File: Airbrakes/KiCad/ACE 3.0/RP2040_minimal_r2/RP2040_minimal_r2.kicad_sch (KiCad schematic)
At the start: 45 parts, among them J1 USB_B_Micro, J2 Conn_01x02, J3 104031-0811, J4 Conn_02x18_Odd_Even, U1 NCP1117-3.3_SOT223, U2 W25Q128JVS, U3 RP2040, U4 BMI088, U5 BMP581, U6 BMM350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

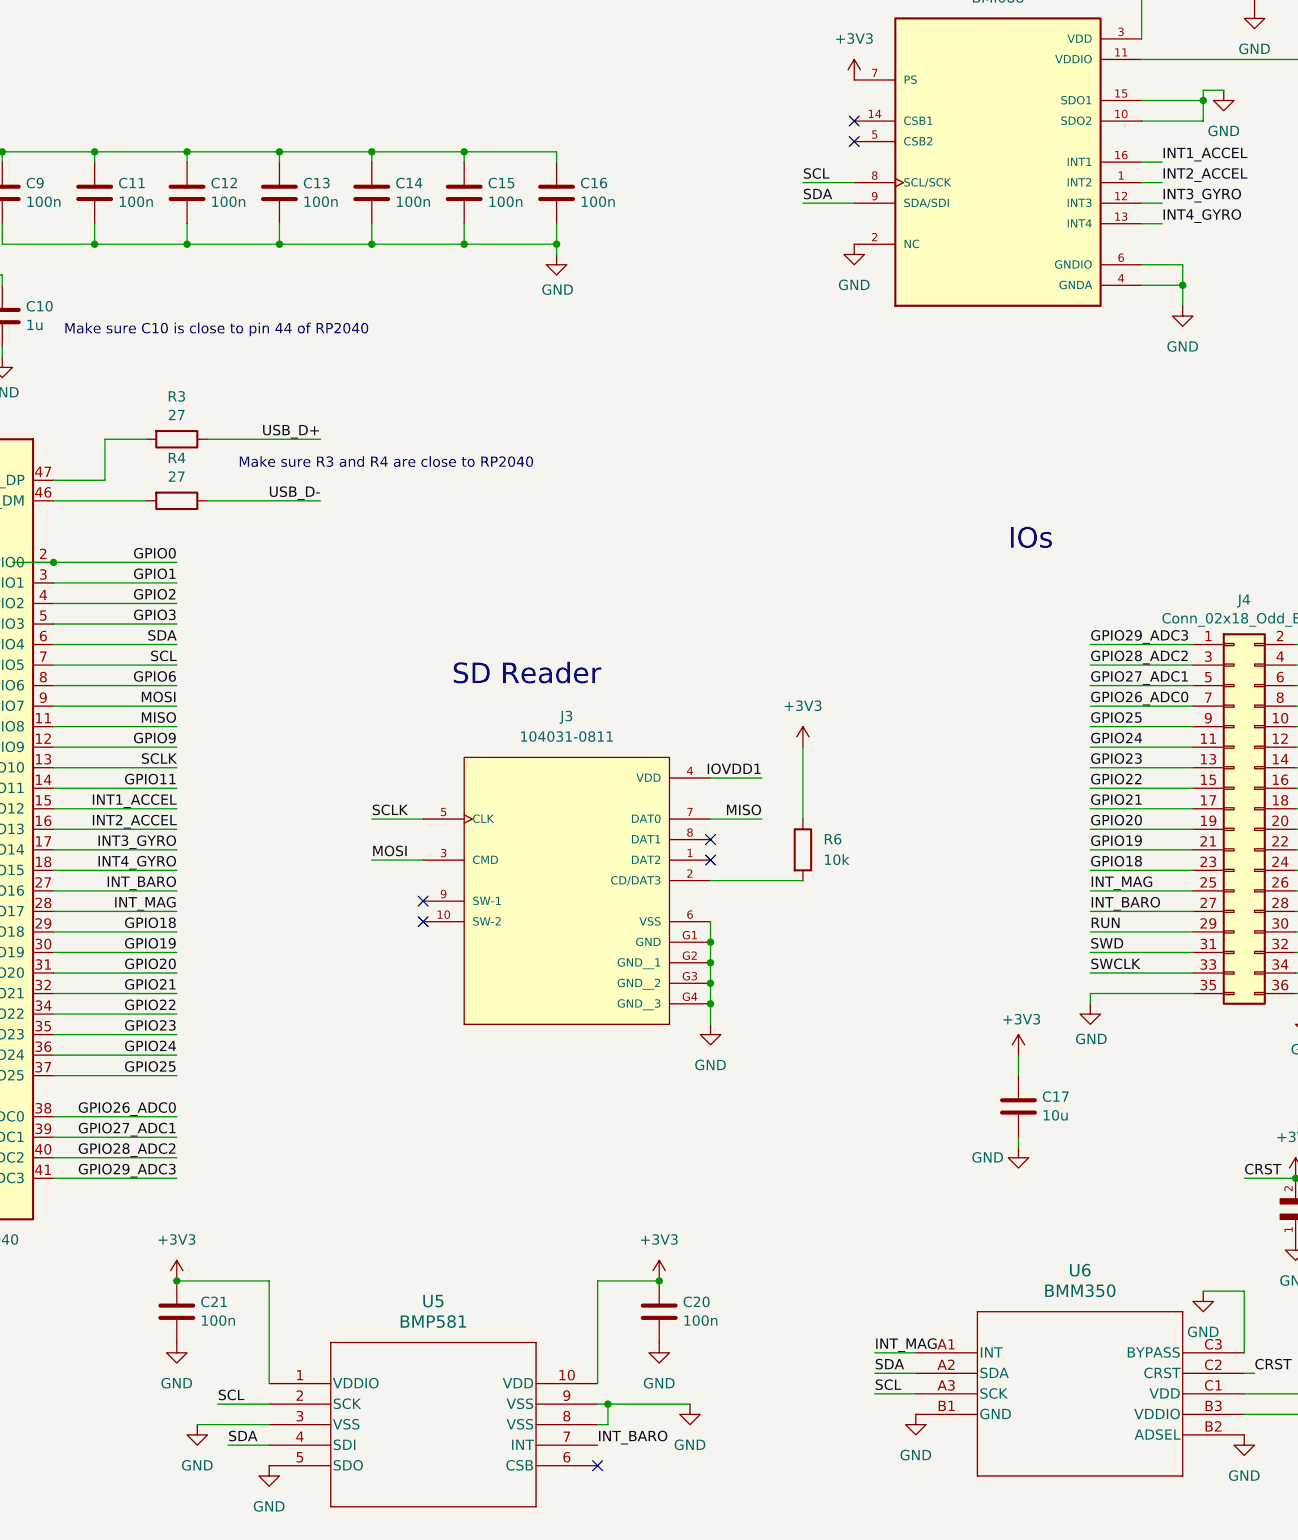
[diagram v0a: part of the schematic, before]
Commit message: Update footprint refs
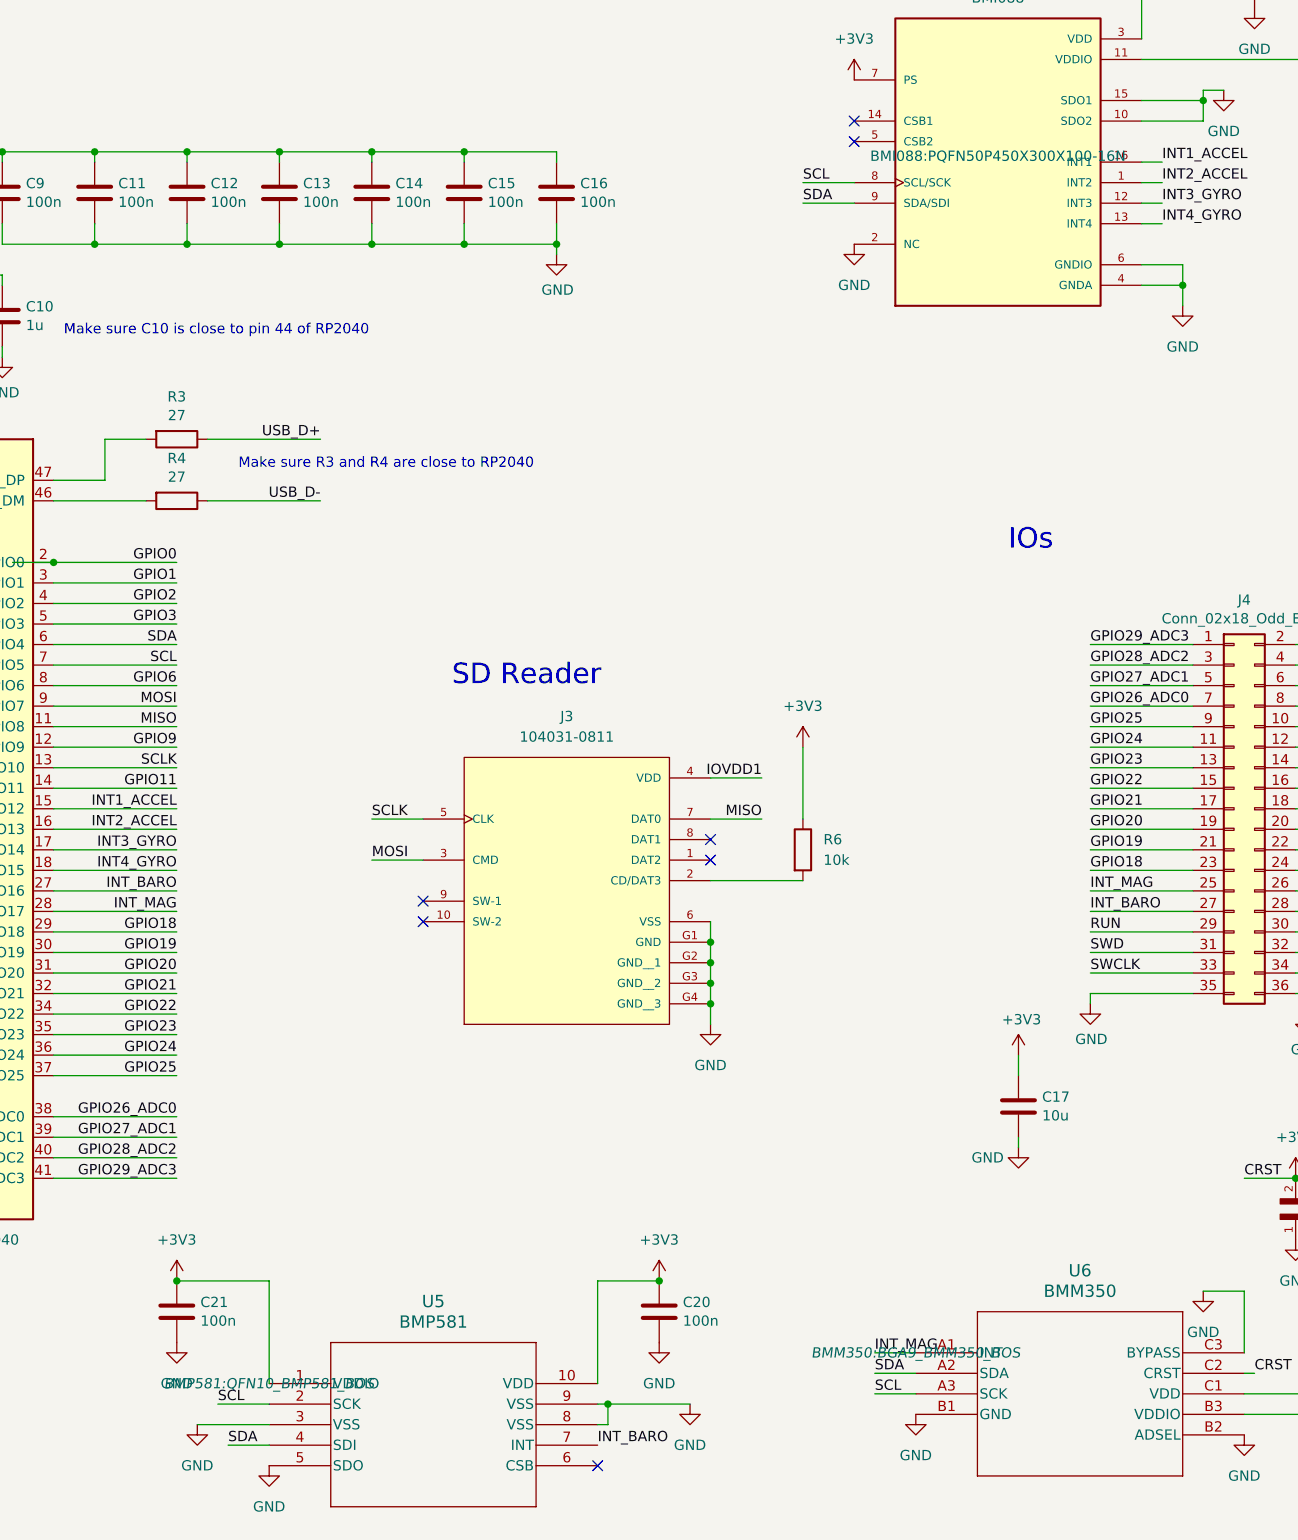
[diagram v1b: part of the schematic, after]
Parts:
- U5: footprint QFN10_BMP581_BOS -> BMP581:QFN10_BMP581_BOS
- U6: footprint BGA9_BMM350_BOS -> BMM350:BGA9_BMM350_BOS
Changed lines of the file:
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@@
 			)
 		)
-		(property "Footprint" "BGA9_BMM350_BOS"
+		(property "Footprint" "BMM350:BGA9_BMM350_BOS"
 			(at 336.55 209.55 0)
 			(effects
@@
 					(italic yes)
 				)
-				(hide yes)
 			)
 		)
@@
 				)
 				(justify bottom)
-				(hide yes)
 			)
 		)
@@
 			)
 		)
-		(property "Footprint" "QFN10_BMP581_BOS"
+		(property "Footprint" "BMP581:QFN10_BMP581_BOS"
 			(at 256.54 213.36 0)
 			(effects
@@
 					(italic yes)
 				)
-				(hide yes)
-			)
-		)
+			)
+		)

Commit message: buttons
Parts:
- removed J2: Conn_01x02, Connector_PinHeader_2.54mm:PinHeader_1x02_P2.54mm_Vertical, symbol Connector_Generic:Conn_01x02
- added U7, U8: B3U-1000P, Button_Switch_SMD:SW_SPST_B3U-1000P, symbol BOOT_Button:B3U-1000P
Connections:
- net GND: now also U7.1, U8.1
- net RUN: now also U8.2
- net ~{USB_BOOT}: now also U7.2
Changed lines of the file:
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@@
 	)
 	(junction
+		(at 142.24 165.1)
+		(diameter 0)
+		(color 0 0 0 0)
+	)
+	(junction
 		(at 384.81 144.78)
 		(diameter 0)
@@
 	(wire
 		(pts
-			(xy 166.37 165.1) (xy 152.4 165.1)
+			(xy 166.37 165.1) (xy 142.24 165.1)
 		)
 		(stroke
@@
 	(wire
 		(pts
-			(xy 31.75 128.27) (xy 33.02 128.27)
-		)
-		(stroke
-			(width 0)
-			(type default)
-		)
-	)
-	(wire
-		(pts
 			(xy 234.95 60.96) (xy 246.38 60.96)
 		)
@@
 	(wire
 		(pts
+			(xy 142.24 165.1) (xy 134.62 165.1)
+		)
+		(stroke
+			(width 0)
+			(type default)
+		)
+	)
+	(wire
+		(pts
 			(xy 104.14 102.87) (xy 104.14 101.6)
 		)
@@
 	(wire
 		(pts
-			(xy 33.02 128.27) (xy 33.02 129.54)
-		)
-		(stroke
-			(width 0)
-			(type default)
-		)
-	)
-	(wire
-		(pts
 			(xy 383.54 149.86) (xy 384.81 149.86)
 		)
@@
 	)
 	(label "RUN"
-		(at 152.4 165.1 0)
+		(at 134.62 165.1 0)
 		(fields_autoplaced yes)
 		(effects
@@
 	)
 	(symbol
-		(lib_id "Connector_Generic:Conn_01x02")
-		(at 26.67 125.73 0)
-		(mirror y)
-		(unit 1)
-		(exclude_from_sim no)
-		(in_bom yes)
-		(on_board yes)
-		(dnp no)
-		(property "Reference" "J2"
-			(at 25.4 121.92 0)
-			(effects
-				(font
-					(size 1.27 1.27)
-				)
-			)
-		)
-		(property "Value" "Conn_01x02"
-			(at 25.4 132.08 0)
-			(effects
-				(font
-					(size 1.27 1.27)
-				)
-			)
-		)
-		(property "Footprint" "Connector_PinHeader_2.54mm:PinHeader_1x02_P2.54mm_Vertical"
-			(at 26.67 125.73 0)
-			(effects
-				(font
-					(size 1.27 1.27)
-				)
-				(hide yes)
-			)
-		)
-		(property "Datasheet" "~"
-			(at 26.67 125.73 0)
-			(effects
-				(font
-					(size 1.27 1.27)
-				)
-				(hide yes)
-			)
-		)
-		(property "Description" ""
-			(at 26.67 125.73 0)
-			(effects
-				(font
-					(size 1.27 1.27)
-				)
-				(hide yes)
-			)
-		)
-		(pin "1"
-		)
-		(pin "2"
-		)
-		(instances
-			(project "RP2040_minimal_r2"
-				(path "/8c0b3d8b-46d3-4173-ab1e-a61765f77d61"
-					(reference "J2")
-					(unit 1)
-				)
-			)
-		)
-	)
-	(symbol
 		(lib_id "power:GND")
-		(at 33.02 129.54 0)
+		(at 31.75 166.37 0)
 		(unit 1)
 		(exclude_from_sim no)
@@
 		(dnp no)
 		(property "Reference" "#PWR02"
-			(at 33.02 135.89 0)
+			(at 31.75 172.72 0)
 			(effects
 				(font
@@
 		)
 		(property "Value" "GND"
-			(at 33.147 133.9342 0)
+			(at 31.877 170.7642 0)
 			(effects
 				(font
@@
 		)
 		(property "Footprint" ""
-			(at 33.02 129.54 0)
+			(at 31.75 166.37 0)
 			(effects
 				(font
@@
 		)
 		(property "Datasheet" ""
-			(at 33.02 129.54 0)
+			(at 31.75 166.37 0)
 			(effects
 				(font
@@
 		)
 		(property "Description" ""
-			(at 33.02 129.54 0)
+			(at 31.75 166.37 0)
 			(effects
 				(font
@@
 	)
 	(symbol
+		(lib_id "power:GND")
+		(at 142.24 205.74 0)
+		(unit 1)
+		(exclude_from_sim no)
+		(in_bom yes)
+		(on_board yes)
+		(dnp no)
+		(property "Reference" "#PWR021"
+			(at 142.24 212.09 0)
+			(effects
+				(font
+					(size 1.27 1.27)
+				)
+				(hide yes)
+			)
+		)
+		(property "Value" "GND"
+			(at 142.367 210.1342 0)
+			(effects
+				(font
+					(size 1.27 1.27)
+				)
+			)
+		)
+		(property "Footprint" ""
+			(at 142.24 205.74 0)
+			(effects
+				(font
+					(size 1.27 1.27)
+				)
+				(hide yes)
+			)
+		)
+		(property "Datasheet" ""
+			(at 142.24 205.74 0)
+			(effects
+				(font
+					(size 1.27 1.27)
+				)
+				(hide yes)
+			)
+		)
+		(property "Description" ""
+			(at 142.24 205.74 0)
+			(effects
+				(font
+					(size 1.27 1.27)
+				)
+				(hide yes)
+			)
+		)
+		(pin "1"
+		)
+		(instances
+			(project "RP2040_minimal_r2"
+				(path "/8c0b3d8b-46d3-4173-ab1e-a61765f77d61"
+					(reference "#PWR021")
+					(unit 1)
+				)
+			)
+		)
+	)
+	(symbol
 		(lib_name "GND_5")
 		(lib_id "power:GND")
@@
 	)
 	(symbol
+		(lib_id "BOOT_Button:B3U-1000P")
+		(at 31.75 166.37 90)
+		(unit 1)
+		(exclude_from_sim no)
+		(in_bom yes)
+		(on_board yes)
+		(dnp no)
+		(fields_autoplaced yes)
+		(property "Reference" "U7"
+			(at 38.1 144.7799 90)
+			(effects
+				(font
+					(size 1.524 1.524)
+				)
+				(justify right)
+			)
+		)
+		(property "Value" "B3U-1000P"
+			(at 38.1 147.3199 90)
+			(effects
+				(font
+					(size 1.524 1.524)
+				)
+				(justify right)
+			)
+		)
+		(property "Footprint" "Button_Switch_SMD:SW_SPST_B3U-1000P"
+			(at 31.75 166.37 0)
+			(effects
+				(font
+					(size 1.27 1.27)
+					(italic yes)
+				)
+				(hide yes)
+			)
+		)
+		(property "Datasheet" "B3U-1000P"
+			(at 31.75 166.37 0)
+			(effects
+				(font
+					(size 1.27 1.27)
+					(italic yes)
+				)
+				(hide yes)
+			)
+		)
+		(property "Description" ""
+			(at 31.75 166.37 0)
+			(effects
+				(font
+					(size 1.27 1.27)
+				)
+				(hide yes)
+			)
+		)
+		(pin "2"
+		)
+		(pin "1"
+		)
+		(instances
+			(project "RP2040_minimal_r2"
+				(path "/8c0b3d8b-46d3-4173-ab1e-a61765f77d61"
+					(reference "U7")
+					(unit 1)
+				)
+			)
+		)
+	)
+	(symbol
 		(lib_id "Device:C")
 		(at 389.89 58.42 0)
@@
 					(unit 1)
 				)
+			)
+		)
+	)
+	(symbol
+		(lib_id "BOOT_Button:B3U-1000P")
+		(at 142.24 205.74 90)
+		(unit 1)
+		(exclude_from_sim no)
+		(in_bom yes)
+		(on_board yes)
+		(dnp no)
+		(fields_autoplaced yes)
+		(property "Reference" "U8"
+			(at 148.59 184.1499 90)
+			(effects
+				(font
+					(size 1.524 1.524)
+				)
+				(justify right)
+			)
+		)
+		(property "Value" "B3U-1000P"
+			(at 148.59 186.6899 90)
+			(effects
+				(font
+					(size 1.524 1.524)
+				)
+				(justify right)
+			)
+		)
+		(property "Footprint" "Button_Switch_SMD:SW_SPST_B3U-1000P"
+			(at 142.24 205.74 0)
+			(effects
+				(font
+					(size 1.27 1.27)
+					(italic yes)
+				)
+				(hide yes)
+			)
+		)
+		(property "Datasheet" "B3U-1000P"
+			(at 142.24 205.74 0)
+			(effects
+				(font
+					(size 1.27 1.27)
+					(italic yes)
+				)
+				(hide yes)
+			)
+		)
+		(property "Description" ""
+			(at 142.24 205.74 0)
+			(effects
+				(font
+					(size 1.27 1.27)
+				)
+				(hide yes)
+			)
+		)
+		(pin "2"
+		)
+		(pin "1"
+		)
+		(instances
+			(project "RP2040_minimal_r2"
+				(path "/8c0b3d8b-46d3-4173-ab1e-a61765f77d61"
+					(reference "U8")
+					(unit 1)
+				)

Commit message: Final review + DRC pass
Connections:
- net GPIO11 is gone; now on net MOSI: U3.14 (GPIO11)
- net +3V3: no longer C24.2, U6.C2 (CRST)
- net MOSI: no longer U3.9 (GPIO7)
- new net CRST: C24.2, U6.C2 (CRST)
- new net GPIO7: U3.9 (GPIO7)
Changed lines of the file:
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@@
 	)
 	(junction
-		(at 383.54 187.96)
-		(diameter 0)
-		(color 0 0 0 0)
-	)
-	(junction
 		(at 201.93 81.28)
 		(diameter 0)
@@
 	)
 	(junction
-		(at 372.11 54.61)
-		(diameter 0)
-		(color 0 0 0 0)
-	)
-	(junction
 		(at 257.81 72.39)
 		(diameter 0)
@@
 	)
 	(junction
+		(at 372.11 57.15)
+		(diameter 0)
+		(color 0 0 0 0)
+	)
+	(junction
 		(at 194.31 81.28)
 		(diameter 0)
@@
 	(wire
 		(pts
-			(xy 374.65 53.34) (xy 372.11 53.34)
-		)
-		(stroke
-			(width 0)
-			(type default)
-		)
-	)
-	(wire
-		(pts
 			(xy 214.63 76.2) (xy 223.52 76.2)
 		)
@@
 	(wire
 		(pts
-			(xy 372.11 53.34) (xy 372.11 54.61)
+			(xy 372.11 57.15) (xy 372.11 54.61)
 		)
 		(stroke
@@
 	(wire
 		(pts
-			(xy 372.11 54.61) (xy 372.11 57.15)
-		)
-		(stroke
-			(width 0)
-			(type default)
-		)
-	)
-	(wire
-		(pts
 			(xy 229.87 165.1) (xy 245.11 165.1)
 		)
@@
 		)
 	)
-	(label "GPIO11"
+	(label "MOSI"
 		(at 245.11 139.7 180)
 		(fields_autoplaced yes)
@@
 		)
 	)
-	(label "MOSI"
+	(label "GPIO7"
 		(at 245.11 129.54 180)
 		(fields_autoplaced yes)
@@
 		(lib_name "GND_2")
 		(lib_id "power:GND")
-		(at 374.65 53.34 0)
+		(at 372.11 57.15 0)
 		(unit 1)
 		(exclude_from_sim no)
@@
 		(on_board yes)
 		(dnp no)
-		(fields_autoplaced yes)
 		(property "Reference" "#PWR031"
-			(at 374.65 59.69 0)
+			(at 372.11 63.5 0)
 			(effects
 				(font
@@
 		)
 		(property "Value" "GND"
-			(at 374.65 58.42 0)
+			(at 376.428 58.674 0)
 			(effects
 				(font
@@
 		)
 		(property "Footprint" ""
-			(at 374.65 53.34 0)
+			(at 372.11 57.15 0)
 			(effects
 				(font
@@
 		)
 		(property "Datasheet" ""
-			(at 374.65 53.34 0)
+			(at 372.11 57.15 0)
 			(effects
 				(font
@@
 		)
 		(property "Description" "Power symbol creates a global label with name \"GND\" , ground"
-			(at 374.65 53.34 0)
+			(at 372.11 57.15 0)
 			(effects
 				(font
@@
 		(on_board yes)
 		(dnp no)
-		(fields_autoplaced yes)
 		(property "Reference" "#PWR035"
 			(at 378.46 49.53 0)
@@
 		)
 		(property "Value" "GND"
-			(at 378.46 48.26 0)
+			(at 382.27 44.958 0)
 			(effects
 				(font
@@
 		(on_board yes)
 		(dnp no)
-		(fields_autoplaced yes)
 		(property "Reference" "U6"
 			(at 356.87 199.39 0)
@@
 		)
 		(property "Footprint" "BMM350:BGA9_BMM350_BOS"
-			(at 336.55 209.55 0)
+			(at 356.87 227.584 0)
 			(effects
 				(font
@@
 	)
 	(symbol
-		(lib_name "+3V3_6")
-		(lib_id "power:+3V3")
-		(at 383.54 187.96 0)
-		(unit 1)
-		(exclude_from_sim no)
-		(in_bom yes)
-		(on_board yes)
-		(dnp no)
-		(fields_autoplaced yes)
-		(property "Reference" "#PWR052"
-			(at 383.54 191.77 0)
-			(effects
-				(font
-					(size 1.27 1.27)
-				)
-				(hide yes)
-			)
-		)
-		(property "Value" "+3V3"
-			(at 383.54 182.88 0)
-			(effects
-				(font
-					(size 1.27 1.27)
-				)
-			)
-		)
-		(property "Footprint" ""
-			(at 383.54 187.96 0)
-			(effects
-				(font
-					(size 1.27 1.27)
-				)
-				(hide yes)
-			)
-		)
-		(property "Datasheet" ""
-			(at 383.54 187.96 0)
-			(effects
-				(font
-					(size 1.27 1.27)
-				)
-				(hide yes)
-			)
-		)
-		(property "Description" "Power symbol creates a global label with name \"+3V3\""
-			(at 383.54 187.96 0)
-			(effects
-				(font
-					(size 1.27 1.27)
-				)
-				(hide yes)
-			)
-		)
-		(pin "1"
-		)
-		(instances
-			(project "RP2040_minimal_r2"
-				(path "/8c0b3d8b-46d3-4173-ab1e-a61765f77d61"
-					(reference "#PWR052")
-					(unit 1)
-				)
-			)
-		)
-	)
-	(symbol
 		(lib_name "GND_6")
 		(lib_id "power:GND")
@@
 		(on_board yes)
 		(dnp no)
-		(fields_autoplaced yes)
 		(property "Reference" "U4"
 			(at 346.71 39.37 0)
@@
 		)
 		(property "Footprint" "BMI088:PQFN50P450X300X100-16N"
-			(at 346.71 62.23 0)
+			(at 345.44 84.836 0)
 			(effects
 				(font
@@
 		(on_board yes)
 		(dnp no)
-		(fields_autoplaced yes)
 		(property "Reference" "U5"
 			(at 276.86 203.2 0)
@@
 		)
 		(property "Footprint" "BMP581:QFN10_BMP581_BOS"
-			(at 256.54 213.36 0)
+			(at 276.606 231.14 0)
 			(effects
 				(font
